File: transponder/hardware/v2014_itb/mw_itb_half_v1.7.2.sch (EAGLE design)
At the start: 31 parts, among them SW1 SWITCH_SPST-KMT0, SW2 SWITCH_SPST-KMT0

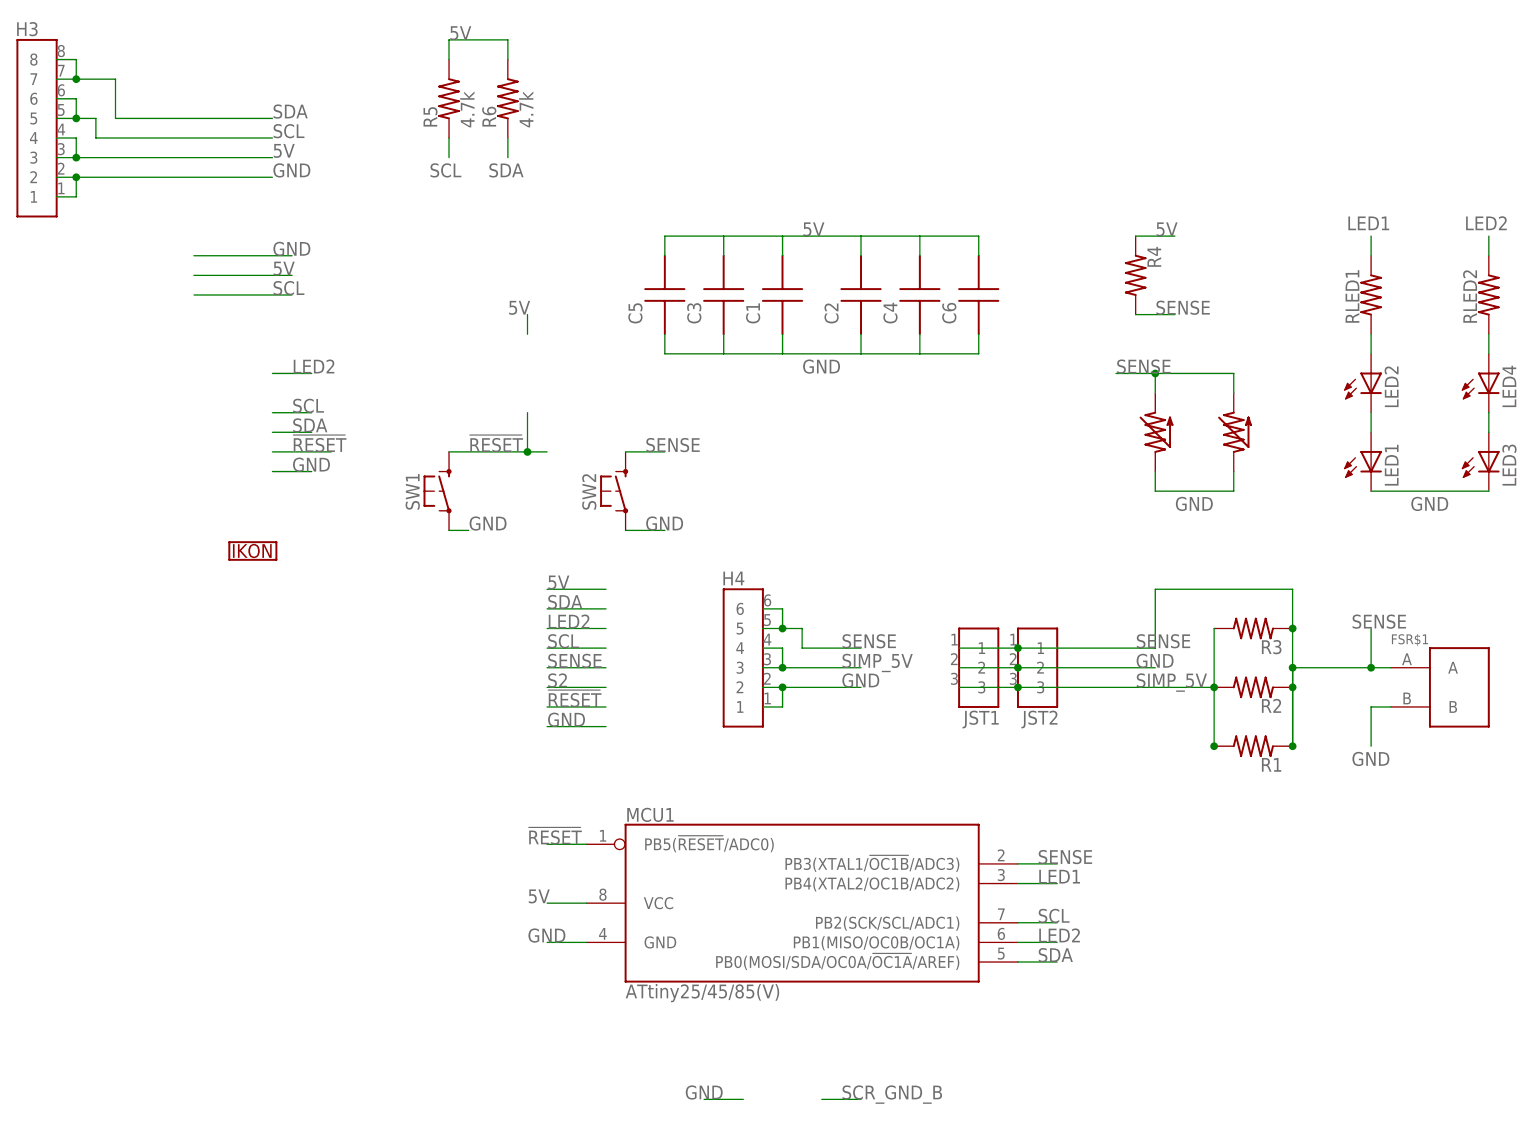
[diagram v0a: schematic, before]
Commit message: Small updates to mw_itb design files.  Basically changed silkscreen for LEDs and added additional button footprint for slightly larger and significantly less expensive TL3315 pushbuttons from E-Switch.   Silkscreen of C&K Components KMT0 footprint was slightly modified to permit it being nested inside new switch footprint.
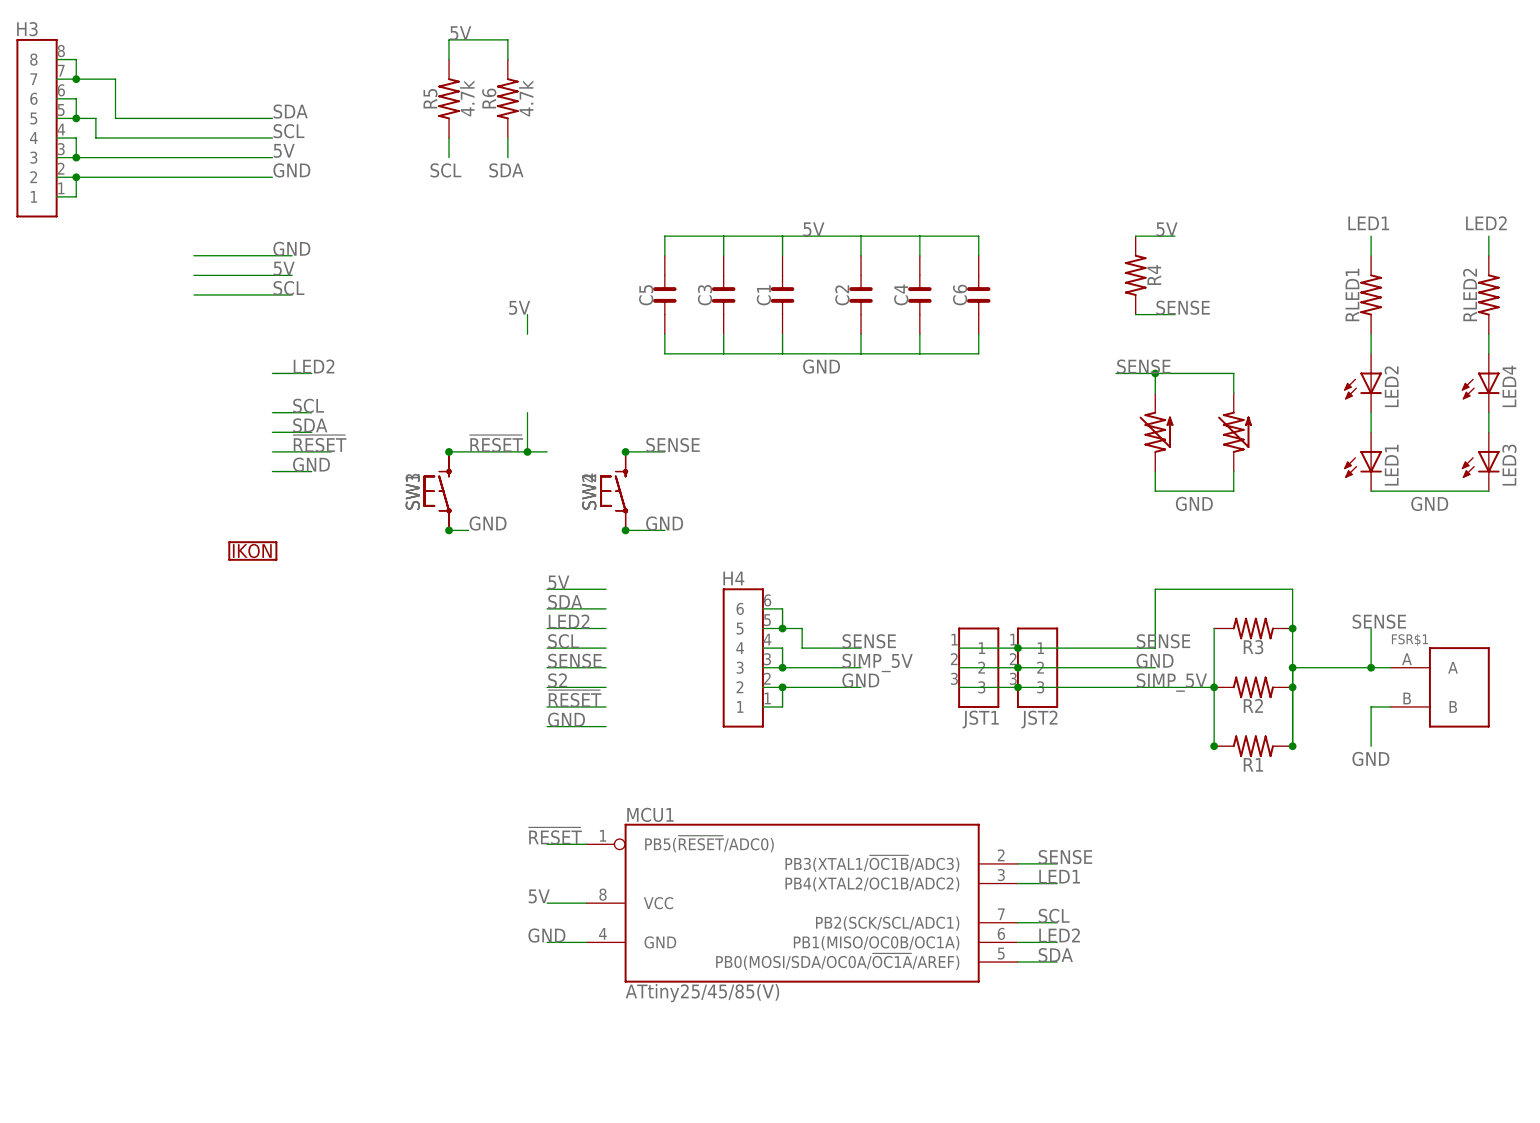
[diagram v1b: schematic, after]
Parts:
- added SW3, SW4: SWITCH_SPST-TL3315, NaN:SWITCH_SPST-TL3315
- C1, C2: device NaN:CAPACITOR1206 -> NaN:CAPACITOR-1206
- C3, C4: device NaN:CAPACITOR0805 -> NaN:CAPACITOR-0805
- C5, C6: device NaN:CAPACITOR0603 -> NaN:CAPACITOR-0603
- R1: device NaN:RESISTOR1206 -> NaN:RESISTOR-1206
- R2: device NaN:RESISTOR0805 -> NaN:RESISTOR-0805
- R3, R4, R5, R6, RLED1, RLED2: device NaN:RESISTOR0603 -> NaN:RESISTOR-0603
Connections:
- net !RESET: now also SW3.1
- net 5V: now also C1.P$2, C2.P$2, C3.P$2, C4.P$2, C5.P$2, C6.P$2; no longer C1.P$1, C2.P$1, C3.P$1, C4.P$1, C5.P$1, C6.P$1
- net GND: now also C1.P$1, C2.P$1, C3.P$1, C4.P$1, C5.P$1, C6.P$1, SW3.2, SW4.2; no longer C1.P$2, C2.P$2, C3.P$2, C4.P$2, C5.P$2, C6.P$2
- net SENSE: now also SW4.1
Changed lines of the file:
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@@
 <part name="U$9" library="NaN" deviceset="FSR_PINS" device="JUMBO_SMD" value="FSR_PINS"/>
 <part name="U$10" library="NaN" deviceset="FSR_PINS" device="JUMBO_SMD" value="FSR_PINS"/>
-<part name="RLED1" library="NaN" deviceset="RESISTOR" device="0603"/>
-<part name="RLED2" library="NaN" deviceset="RESISTOR" device="0603"/>
-<part name="C1" library="NaN" deviceset="CAPACITOR" device="1206"/>
-<part name="C2" library="NaN" deviceset="CAPACITOR" device="1206"/>
+<part name="RLED1" library="NaN" deviceset="RESISTOR" device="-0603"/>
+<part name="RLED2" library="NaN" deviceset="RESISTOR" device="-0603"/>
+<part name="C1" library="NaN" deviceset="CAPACITOR" device="-1206"/>
+<part name="C2" library="NaN" deviceset="CAPACITOR" device="-1206"/>
 <part name="U$11" library="NaN" deviceset="IKON" device="LEARNING-20MIL"/>
 <part name="FSR$1" library="NaN" deviceset="FSR_PAD" device="88X44_P2B"/>
-<part name="R1" library="NaN" deviceset="RESISTOR" device="1206"/>
-<part name="R2" library="NaN" deviceset="RESISTOR" device="0805"/>
-<part name="C3" library="NaN" deviceset="CAPACITOR" device="0805"/>
-<part name="C4" library="NaN" deviceset="CAPACITOR" device="0805"/>
-<part name="C5" library="NaN" deviceset="CAPACITOR" device="0603"/>
-<part name="C6" library="NaN" deviceset="CAPACITOR" device="0603"/>
-<part name="R3" library="NaN" deviceset="RESISTOR" device="0603"/>
-<part name="R4" library="NaN" deviceset="RESISTOR" device="0603"/>
+<part name="R1" library="NaN" deviceset="RESISTOR" device="-1206"/>
+<part name="R2" library="NaN" deviceset="RESISTOR" device="-0805"/>
+<part name="C3" library="NaN" deviceset="CAPACITOR" device="-0805"/>
+<part name="C4" library="NaN" deviceset="CAPACITOR" device="-0805"/>
+<part name="C5" library="NaN" deviceset="CAPACITOR" device="-0603"/>
+<part name="C6" library="NaN" deviceset="CAPACITOR" device="-0603"/>
+<part name="R3" library="NaN" deviceset="RESISTOR" device="-0603"/>
+<part name="R4" library="NaN" deviceset="RESISTOR" device="-0603"/>
 <part name="JST1" library="NaN" deviceset="JST-3" device="-PH-SMD-TOP"/>
 <part name="JST2" library="NaN" deviceset="JST-3" device="-PH-SMD-TOP"/>
-<part name="R5" library="NaN" deviceset="RESISTOR" device="0603" value="4.7k"/>
-<part name="R6" library="NaN" deviceset="RESISTOR" device="0603" value="4.7k"/>
+<part name="R5" library="NaN" deviceset="RESISTOR" device="-0603" value="4.7k"/>
+<part name="R6" library="NaN" deviceset="RESISTOR" device="-0603" value="4.7k"/>
 <part name="SW1" library="NaN" deviceset="SWITCH_SPST" device="-KMT0"/>
 <part name="SW2" library="NaN" deviceset="SWITCH_SPST" device="-KMT0"/>
@@
 <part name="H3" library="NaN" deviceset="HEADER_8P" device="-0.1&quot;_2X4-SMD-SULLINS"/>
 <part name="H4" library="NaN" deviceset="HEADER_6P" device="-0.1&quot;_2X3-SMD-SULLINS"/>
+<part name="SW3" library="NaN" deviceset="SWITCH_SPST" device="-TL3315" value="SWITCH_SPST-TL3315"/>
+<part name="SW4" library="NaN" deviceset="SWITCH_SPST" device="-TL3315" value="SWITCH_SPST-TL3315"/>
 </parts>
 <sheets>
@@
 <instance part="RLED1" gate="G$1" x="109.22" y="50.8" rot="R90"/>
 <instance part="RLED2" gate="G$1" x="124.46" y="50.8" rot="R90"/>
-<instance part="C1" gate="G$1" x="33.02" y="50.8"/>
-<instance part="C2" gate="G$1" x="43.18" y="50.8"/>
+<instance part="C1" gate="G$1" x="33.02" y="50.8" rot="R90"/>
+<instance part="C2" gate="G$1" x="43.18" y="50.8" rot="R90"/>
 <instance part="U$11" gate="G$1" x="-35.56" y="17.78"/>
 <instance part="FSR$1" gate="G$1" x="116.84" y="0"/>
 <instance part="R1" gate="G$1" x="93.98" y="-7.62" rot="R180"/>
 <instance part="R2" gate="G$1" x="93.98" y="0" rot="R180"/>
-<instance part="C3" gate="G$1" x="25.4" y="50.8"/>
-<instance part="C4" gate="G$1" x="50.8" y="50.8"/>
-<instance part="C5" gate="G$1" x="17.78" y="50.8"/>
-<instance part="C6" gate="G$1" x="58.42" y="50.8"/>
+<instance part="C3" gate="G$1" x="25.4" y="50.8" rot="R90"/>
+<instance part="C4" gate="G$1" x="50.8" y="50.8" rot="R90"/>
+<instance part="C5" gate="G$1" x="17.78" y="50.8" rot="R90"/>
+<instance part="C6" gate="G$1" x="58.42" y="50.8" rot="R90"/>
 <instance part="R3" gate="G$1" x="93.98" y="7.62" rot="R180"/>
 <instance part="R4" gate="G$1" x="78.74" y="53.34" rot="R270"/>
@@
 <instance part="H3" gate="G$1" x="-60.96" y="73.66"/>
 <instance part="H4" gate="G$1" x="30.48" y="5.08"/>
+<instance part="SW3" gate="G$1" x="-10.16" y="25.4" rot="R90"/>
+<instance part="SW4" gate="G$1" x="12.7" y="25.4" rot="R90"/>
 </instances>
 <busses>
@@
 <wire x1="58.42" y1="43.18" x2="58.42" y2="45.72" width="0.1524" layer="91"/>
 <label x="35.56" y="40.64" size="1.778" layer="95"/>
-<pinref part="C1" gate="G$1" pin="P$2"/>
-<pinref part="C2" gate="G$1" pin="P$2"/>
-<pinref part="C3" gate="G$1" pin="P$2"/>
-<pinref part="C4" gate="G$1" pin="P$2"/>
-<pinref part="C5" gate="G$1" pin="P$2"/>
-<pinref part="C6" gate="G$1" pin="P$2"/>
+<pinref part="C1" gate="G$1" pin="P$1"/>
+<pinref part="C2" gate="G$1" pin="P$1"/>
+<pinref part="C3" gate="G$1" pin="P$1"/>
+<pinref part="C4" gate="G$1" pin="P$1"/>
+<pinref part="C5" gate="G$1" pin="P$1"/>
+<pinref part="C6" gate="G$1" pin="P$1"/>
 </segment>
 <segment>
@@
 <label x="0" y="-33.02" size="1.778" layer="95"/>
 <pinref part="MCU1" gate="G$1" pin="GND"/>
-</segment>
-<segment>
-<wire x1="27.94" y1="-53.34" x2="22.86" y2="-53.34" width="0.1524" layer="91"/>
-<label x="25.4" y="-53.34" size="1.778" layer="95" rot="MR0"/>
 </segment>
 <segment>
@@
 <wire x1="-10.16" y1="20.32" x2="-7.62" y2="20.32" width="0.1524" layer="91"/>
 <label x="-7.62" y="20.32" size="1.778" layer="95"/>
+<pinref part="SW3" gate="G$1" pin="2"/>
+<junction x="-10.16" y="20.32"/>
 </segment>
 <segment>
@@
 <wire x1="12.7" y1="20.32" x2="17.78" y2="20.32" width="0.1524" layer="91"/>
 <label x="15.24" y="20.32" size="1.778" layer="95"/>
+<pinref part="SW4" gate="G$1" pin="2"/>
+<junction x="12.7" y="20.32"/>
 </segment>
 <segment>
@@
 <wire x1="58.42" y1="58.42" x2="58.42" y2="55.88" width="0.1524" layer="91"/>
 <label x="35.56" y="58.42" size="1.778" layer="95"/>
-<pinref part="C1" gate="G$1" pin="P$1"/>
-<pinref part="C2" gate="G$1" pin="P$1"/>
-<pinref part="C3" gate="G$1" pin="P$1"/>
-<pinref part="C4" gate="G$1" pin="P$1"/>
-<pinref part="C5" gate="G$1" pin="P$1"/>
-<pinref part="C6" gate="G$1" pin="P$1"/>
+<pinref part="C1" gate="G$1" pin="P$2"/>
+<pinref part="C2" gate="G$1" pin="P$2"/>
+<pinref part="C3" gate="G$1" pin="P$2"/>
+<pinref part="C4" gate="G$1" pin="P$2"/>
+<pinref part="C5" gate="G$1" pin="P$2"/>
+<pinref part="C6" gate="G$1" pin="P$2"/>
 </segment>
 <segment>
@@
 <label x="-7.62" y="30.48" size="1.778" layer="95"/>
 <pinref part="SW1" gate="G$1" pin="1"/>
+<pinref part="SW3" gate="G$1" pin="1"/>
+<junction x="-10.16" y="30.48"/>
 </segment>
 <segment>
@@
 <wire x1="12.7" y1="30.48" x2="17.78" y2="30.48" width="0.1524" layer="91"/>
 <label x="15.24" y="30.48" size="1.778" layer="95"/>
+<pinref part="SW4" gate="G$1" pin="1"/>
+<junction x="12.7" y="30.48"/>
 </segment>
 <segment>
@@
 </segment>
 </net>
-<net name="SCR_GND_B" class="0">
-<segment>
-<wire x1="38.1" y1="-53.34" x2="43.18" y2="-53.34" width="0.1524" layer="91"/>
-<label x="40.64" y="-53.34" size="1.778" layer="95"/>
-</segment>
-</net>
